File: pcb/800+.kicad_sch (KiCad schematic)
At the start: 37 parts, among them J1 2inch LCD, J6 ESP_JTAG, J7 ESP_PROG, Q1 AO3401A, Q2 AO3401A, Q3 AO3401A, Q4 AO3401A, U12 VEML7700-TR, U2 ESP32-S3-WROOM-1U, U7 TSOP75340TT

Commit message: readme updates
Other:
- note added: "Design updates: ESP32 6 free GPIO MSP430 0 free gpio Connector and standard lipo battery for alternative ESP32 JTAG connector by the esp32, remove case to access MSP430 SWD to battery access cutout, more useful Rotate backlight led foot prints to maximize clearance to holes for better routing Add/fix courtyards to custom footprints Add mic to design? Add inertial measurement, tilt shake tap remot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"
- note removed: "Update cradel footprint to support stock and generic jst 1.25 ESP32 JTAG connector by the esp32, remove case to access MSP430 SWD to battery access cutout, more useful Rotate backlight led foot prints to maximize clearance to holes for better routing Add/fix courtyards to custom footprints --------- ESP32 6 free GPIO MSP430 0 free gpio Aliexpress 2.5mm x 5p connector fits battery snuggly, too sho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"
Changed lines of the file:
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@@
     (effects (font (size 1.27 1.27)) (justify left bottom))
   )
-  (text "Update cradel footprint to support stock and generic jst 1.25\nESP32 JTAG connector by the esp32, remove case to access\nMSP430 SWD to battery access cutout, more useful\nRotate backlight led foot prints to maximize clearance to holes for better routing\nAdd/fix courtyards to custom footprints\n\n---------\nESP32 6 free GPIO\nMSP430 0 free gpio\n\nAliexpress 2.5mm x 5p connector fits battery snuggly, too short\nkeep looking for available replacments\n\nAliexprexx cradle jst bigger than stock, mounting pads wider.\nPlug fits Maybe not jst, molex or amphenol?\n\nbattery thermistor, find way to pulse or control supply current\nvref from msp430, one of the port 2 inputs switched briefly.\n\nIs ESP TX to MSP needed?  Removed it,  we will see....\nRolling ball might work as last switch on button matrix\n\nRegular LEDs instead of reverse mount, \n--less holes and cheaper, clearance and 2 reflows.  Tape to mount switch domes more complicated\n--1206 upside down, cheaper, 1 reflow, more hand rework\n--SK6812Mini reverse mount, cheap,  but bigger cutout battery compartment clearance\n--Leds on flex PCB attached to main PCB like the stock EL\n\nTest:\nambient light sensor operation inside case.\n\n"
-    (at 27.94 287.02 0)
+  (text "Design updates:\n\nESP32 6 free GPIO\nMSP430 0 free gpio\n\nConnector and standard lipo battery for alternative\n\nESP32 JTAG connector by the esp32, remove case to access\nMSP430 SWD to battery access cutout, more useful\n\nRotate backlight led foot prints to maximize clearance to holes for better routing\n\nAdd/fix courtyards to custom footprints\n\nAdd mic to design?\n\nAdd inertial measurement, tilt shake tap remote as user inputs\n\nUpdate cradel footprint to support stock and generic jst 1.25\nbattery thermistor, find way to pulse or control supply current\nvref from msp430, one of the port 2 inputs switched briefly.\n\nIs ESP TX to MSP needed?  Removed it,  we will see....\nRolling ball might work as last switch on button matrix\n\nRegular LEDs instead of reverse mount, \n--less holes and cheaper, clearance and 2 reflows.  Tape to mount switch domes more complicated\n--1206 upside down, cheaper, 1 reflow, more hand rework\n--SK6812Mini reverse mount, cheap,  but bigger cutout battery compartment clearance\n--Leds on flex PCB attached to main PCB like the stock EL\n\nDielectric grease on dome switches.  Hold in place until taped, prevent corrosion  but messy\n\nSoftware:\nTest energia/arduino on MSP430 vs bare metal\n\nTest:\npower supply operation and feedback\nambient light sensor operation inside case.\nIR input and output\nIR output LED performance\nAlternate rolling ball for better response\nBattery charging\nFuel gauge\nBuzzer\nPower consumption\n\nOrder:\nJST connector from digikey\nTranslucent white tape to difuse leds\n\nAliexpress 2.5mm x 5p connector fits battery snuggly, too short\nkeep looking for available replacments\n"
+    (at 30.48 331.47 0)
     (effects (font (size 1.27 1.27)) (justify left bottom))
   )

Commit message: update todo and reference info
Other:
- note added: "Design updates: ESP32 6 free GPIO MSP430 -2 free gpio Connector and standard lipo battery for alternative ESP32 JTAG connector by the esp32, remove case to access MSP430 SWD to battery access cutout, more useful Rotate backlight led foot prints to maximize clearance to holes for better routing Add/fix courtyards to custom footprints Add mic to design? 3v3vp power enable pull down? Add inertial me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"
- note removed: "Design updates: ESP32 6 free GPIO MSP430 0 free gpio Connector and standard lipo battery for alternative ESP32 JTAG connector by the esp32, remove case to access MSP430 SWD to battery access cutout, more useful Rotate backlight led foot prints to maximize clearance to holes for better routing Add/fix courtyards to custom footprints Add mic to design? Add inertial measurement, tilt shake tap remot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"

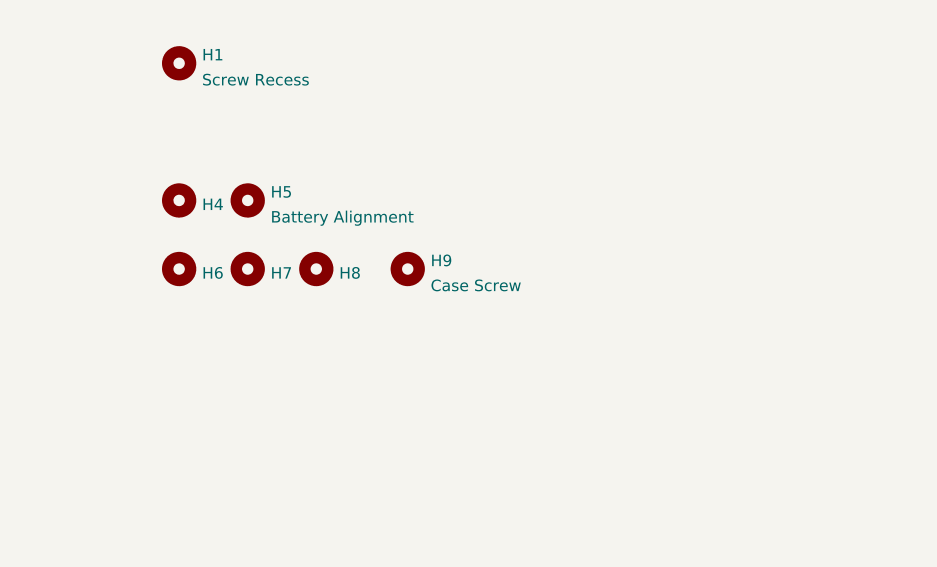
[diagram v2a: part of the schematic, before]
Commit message: update case screws
bottom courtyard added for case screws to account for boss on the case
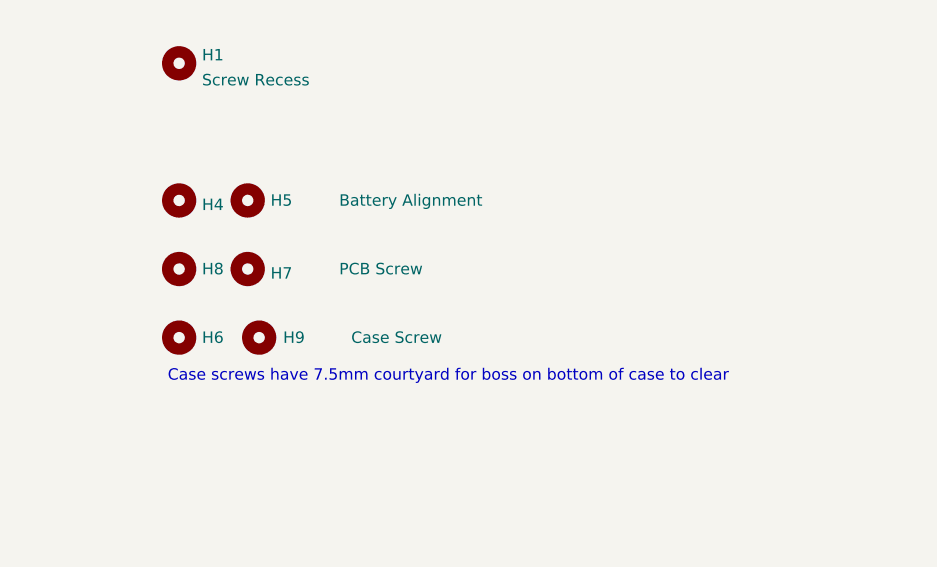
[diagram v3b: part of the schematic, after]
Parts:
- H6, H9: footprint MountingHole:MountingHole_2.2mm_M2 -> 880+:MountingHole_Boss
- H7, H8: value Case Screw -> PCB Screw
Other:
- note added: "Case screws have 7.5mm courtyard for boss on bottom of case to clear"
- moved on the sheet: H6, H8, H9
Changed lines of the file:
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@@
     (effects (font (size 5 5) (thickness 1) bold) (justify left bottom))
+  )
+  (text "Case screws have 7.5mm courtyard for boss on bottom of case to clear"
+    (at 389.89 167.64 0)
+    (effects (font (size 1.27 1.27)) (justify left bottom))
   )
   (text "1.5V 100mA" (at 138.43 55.245 0)
@@
   )
   (symbol (lib_id "Mechanical:MountingHole") (at 398.78 147.32 0) (unit 1)
-    (in_bom yes) (on_board yes) (dnp no) (fields_autoplaced)
-    (property "Reference" "H5" (at 401.32 146.4115 0)
-      (effects (font (size 1.27 1.27)) (justify left))
-    )
-    (property "Value" "Battery Alignment" (at 401.32 149.1866 0)
+    (in_bom yes) (on_board yes) (dnp no)
+    (property "Reference" "H5" (at 401.32 147.32 0)
+      (effects (font (size 1.27 1.27)) (justify left))
+    )
+    (property "Value" "Battery Alignment" (at 408.94 147.32 0)
       (effects (font (size 1.27 1.27)) (justify left))
     )
@@
     )
   )
-  (symbol (lib_id "Mechanical:MountingHole") (at 416.56 154.94 0) (unit 1)
-    (in_bom yes) (on_board yes) (dnp no) (fields_autoplaced)
-    (property "Reference" "H9" (at 419.1 154.0315 0)
-      (effects (font (size 1.27 1.27)) (justify left))
-    )
-    (property "Value" "Case Screw" (at 419.1 156.8066 0)
-      (effects (font (size 1.27 1.27)) (justify left))
-    )
-    (property "Footprint" "MountingHole:MountingHole_2.2mm_M2" (at 416.56 154.94 0)
-      (effects (font (size 1.27 1.27)) hide)
-    )
-    (property "Datasheet" "~" (at 416.56 154.94 0)
+  (symbol (lib_id "Mechanical:MountingHole") (at 400.05 162.56 0) (mirror y) (unit 1)
+    (in_bom yes) (on_board yes) (dnp no)
+    (property "Reference" "H9" (at 405.13 162.56 0)
+      (effects (font (size 1.27 1.27)) (justify left))
+    )
+    (property "Value" "Case Screw" (at 420.37 162.56 0)
+      (effects (font (size 1.27 1.27)) (justify left))
+    )
+    (property "Footprint" "880+:MountingHole_Boss" (at 400.05 162.56 0)
+      (effects (font (size 1.27 1.27)) hide)
+    )
+    (property "Datasheet" "~" (at 400.05 162.56 0)
       (effects (font (size 1.27 1.27)) hide)
     )
@@
   )
   (symbol (lib_id "Mechanical:MountingHole") (at 398.78 154.94 0) (unit 1)
-    (in_bom yes) (on_board yes) (dnp no) (fields_autoplaced)
+    (in_bom yes) (on_board yes) (dnp no)
     (property "Reference" "H7" (at 401.32 155.419 0)
       (effects (font (size 1.27 1.27)) (justify left))
     )
-    (property "Value" "Case Screw" (at 401.32 156.8066 0)
-      (effects (font (size 1.27 1.27)) (justify left) hide)
+    (property "Value" "PCB Screw" (at 408.94 154.94 0)
+      (effects (font (size 1.27 1.27)) (justify left))
     )
     (property "Footprint" "MountingHole:MountingHole_2.2mm_M2" (at 398.78 154.94 0)
@@
     )
   )
-  (symbol (lib_id "Mechanical:MountingHole") (at 391.16 154.94 0) (unit 1)
-    (in_bom yes) (on_board yes) (dnp no) (fields_autoplaced)
-    (property "Reference" "H6" (at 393.7 155.419 0)
-      (effects (font (size 1.27 1.27)) (justify left))
-    )
-    (property "Value" "Case Screw" (at 393.7 156.8066 0)
-      (effects (font (size 1.27 1.27)) (justify left) hide)
-    )
-    (property "Footprint" "MountingHole:MountingHole_2.2mm_M2" (at 391.16 154.94 0)
-      (effects (font (size 1.27 1.27)) hide)
-    )
-    (property "Datasheet" "~" (at 391.16 154.94 0)
+  (symbol (lib_id "Mechanical:MountingHole") (at 391.16 162.56 0) (unit 1)
+    (in_bom yes) (on_board yes) (dnp no) (fields_autoplaced)
+    (property "Reference" "H6" (at 393.7 162.56 0)
+      (effects (font (size 1.27 1.27)) (justify left))
+    )
+    (property "Value" "Case Screw" (at 393.7 164.4266 0)
+      (effects (font (size 1.27 1.27)) (justify left) hide)
+    )
+    (property "Footprint" "880+:MountingHole_Boss" (at 391.16 162.56 0)
+      (effects (font (size 1.27 1.27)) hide)
+    )
+    (property "Datasheet" "~" (at 391.16 162.56 0)
       (effects (font (size 1.27 1.27)) hide)
     )
@@
     )
   )
-  (symbol (lib_id "Mechanical:MountingHole") (at 406.4 154.94 0) (unit 1)
-    (in_bom yes) (on_board yes) (dnp no) (fields_autoplaced)
-    (property "Reference" "H8" (at 408.94 155.419 0)
-      (effects (font (size 1.27 1.27)) (justify left))
-    )
-    (property "Value" "Case Screw" (at 408.94 156.8066 0)
-      (effects (font (size 1.27 1.27)) (justify left) hide)
-    )
-    (property "Footprint" "MountingHole:MountingHole_2.2mm_M2" (at 406.4 154.94 0)
-      (effects (font (size 1.27 1.27)) hide)
-    )
-    (property "Datasheet" "~" (at 406.4 154.94 0)
-      (effects (font (size 1.27 1.27)) hide)
-    )
+  (symbol (lib_id "Mechanical:MountingHole") (at 391.16 154.94 0) (unit 1)
+    (in_bom yes) (on_board yes) (dnp no)
+    (property "Reference" "H8" (at 393.7 154.94 0)
+      (effects (font (size 1.27 1.27)) (justify left))
+    )
+    (property "Value" "PCB Screw" (at 393.7 156.8066 0)
+      (effects (font (size 1.27 1.27)) (justify left) hide)
+    )
+    (property "Footprint" "MountingHole:MountingHole_2.2mm_M2" (at 391.16 154.94 0)
+      (effects (font (size 1.27 1.27)) hide)
+    )
+    (property "Datasheet" "~" (at 391.16 154.94 0)
+      (effects (font (size 1.27 1.27)) hide)
+    )
